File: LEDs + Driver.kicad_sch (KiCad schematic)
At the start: 23 parts, among them U2 LP5860

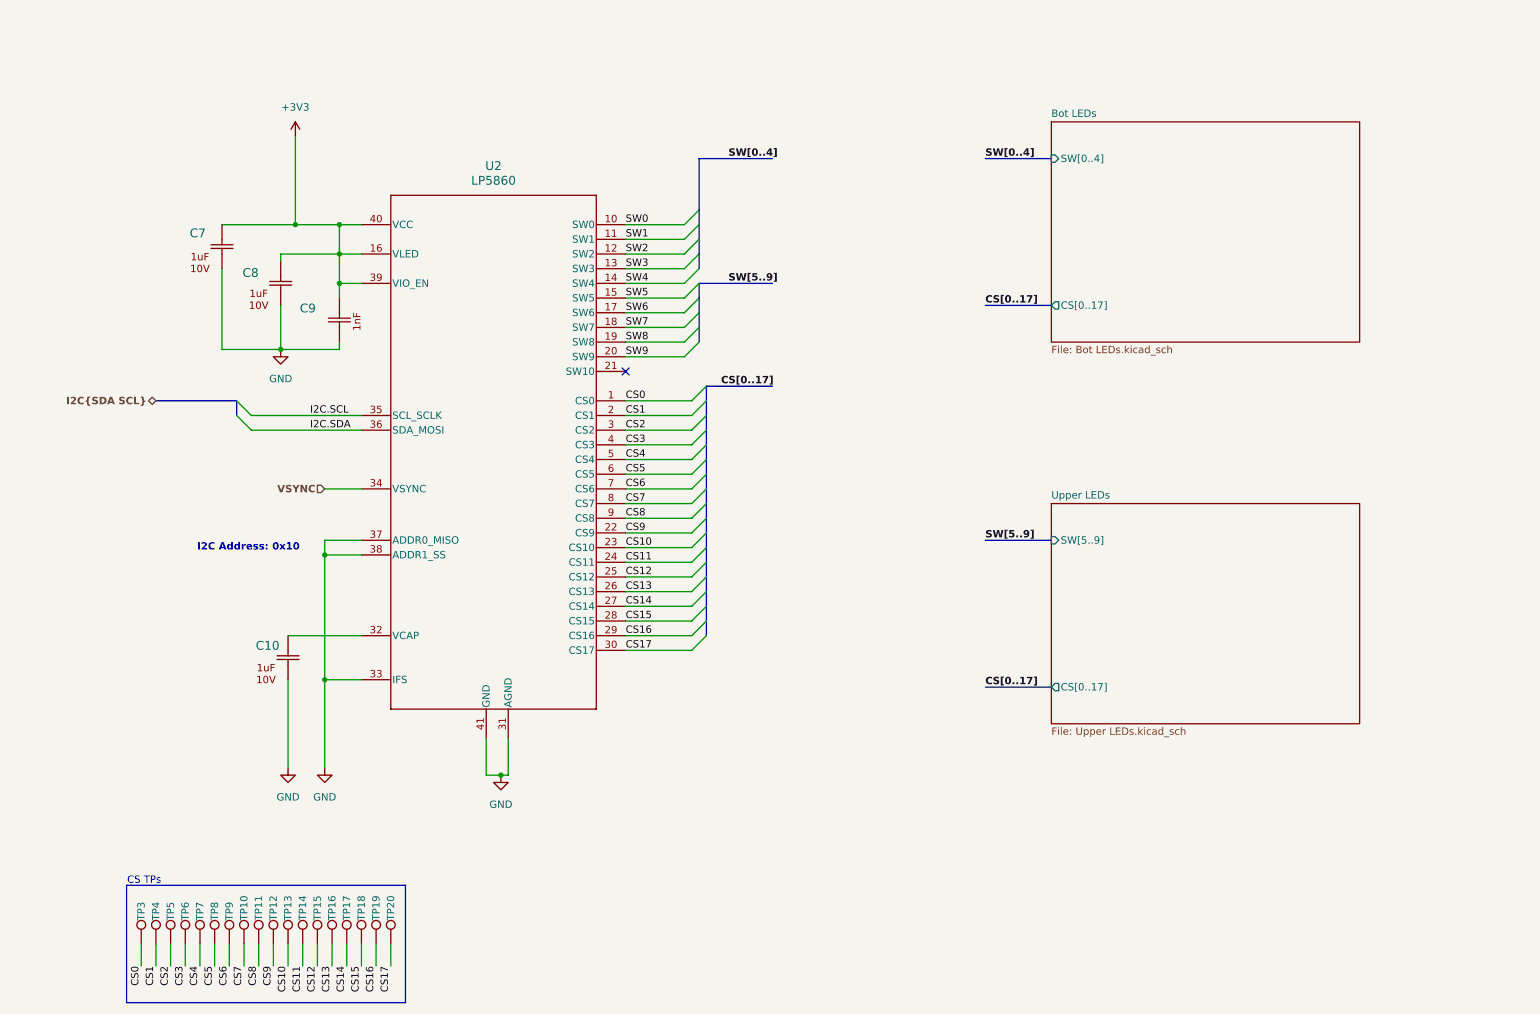
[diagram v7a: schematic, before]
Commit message: Addressed pull-up on NRST. Added GPIO for  VIO_EN. Added comments on schematic and some TPs
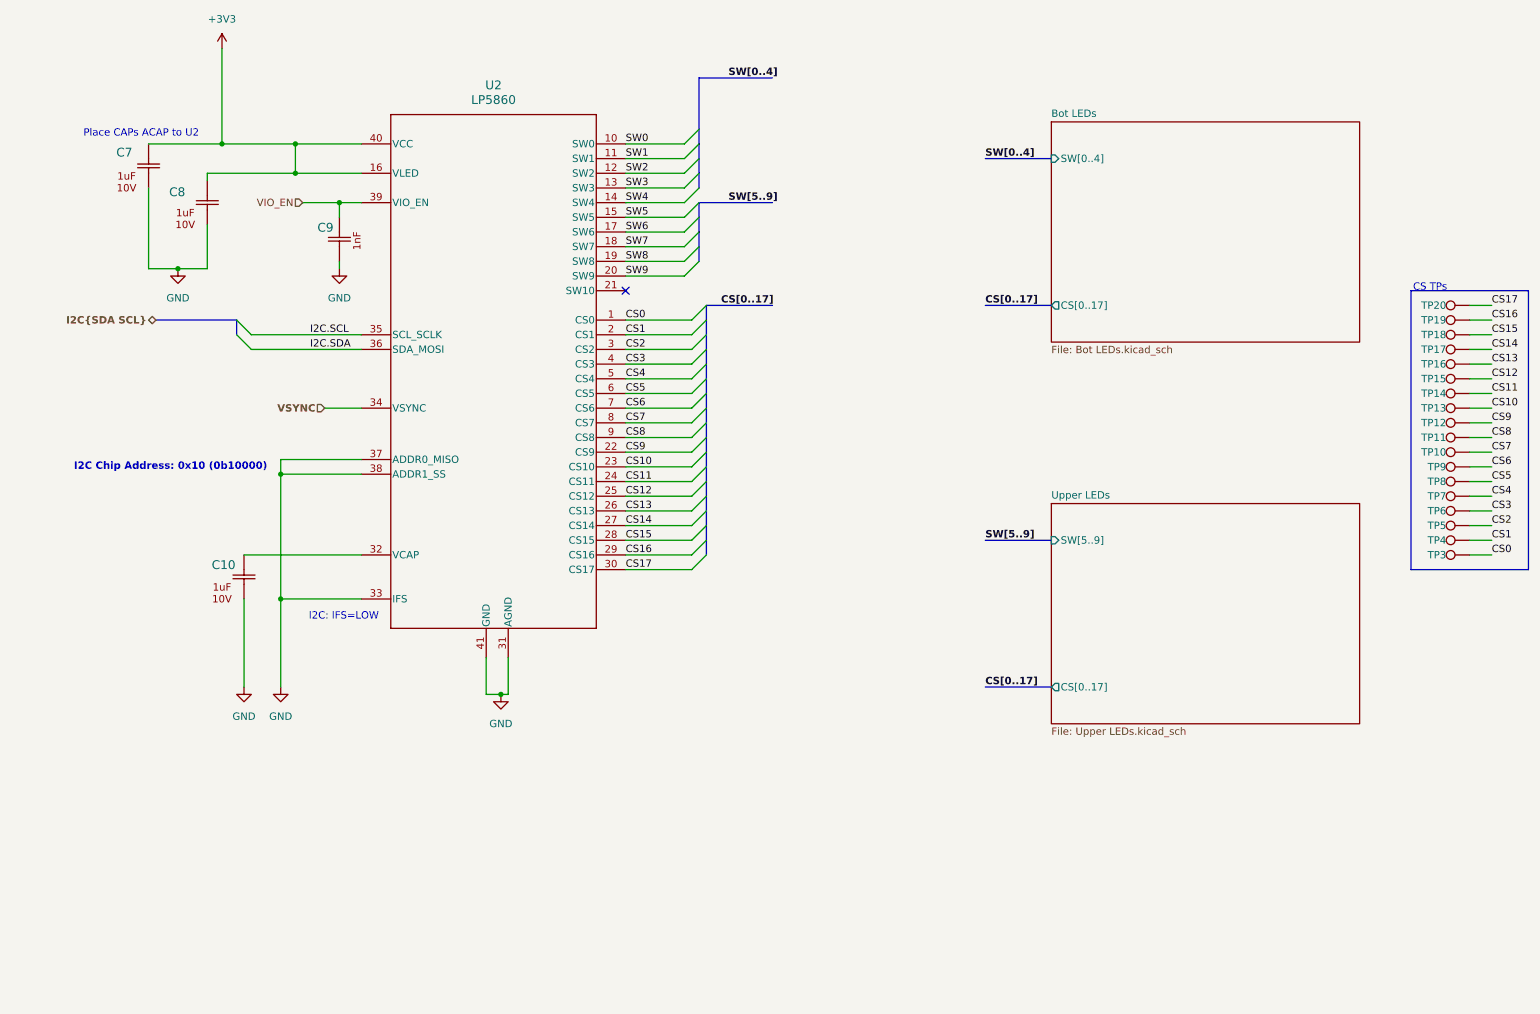
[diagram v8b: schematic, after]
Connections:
- net +3V3: no longer C9.1, U2.39 (VIO_EN)
- new net VIO_EN: C9.1, U2.39 (VIO_EN)
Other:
- note added: "I2C Chip Address: 0x10 (0b10000)"
- note added: "I2C: IFS=LOW"
- note added: "Place CAPs ACAP to U2"
- note removed: "I2C Address: 0x10"
- moved on the sheet: C10, C7, C8, C9, TP10, TP11, TP12, TP13, TP14, TP15, TP16, TP17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
